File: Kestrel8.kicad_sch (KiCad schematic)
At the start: 0 parts

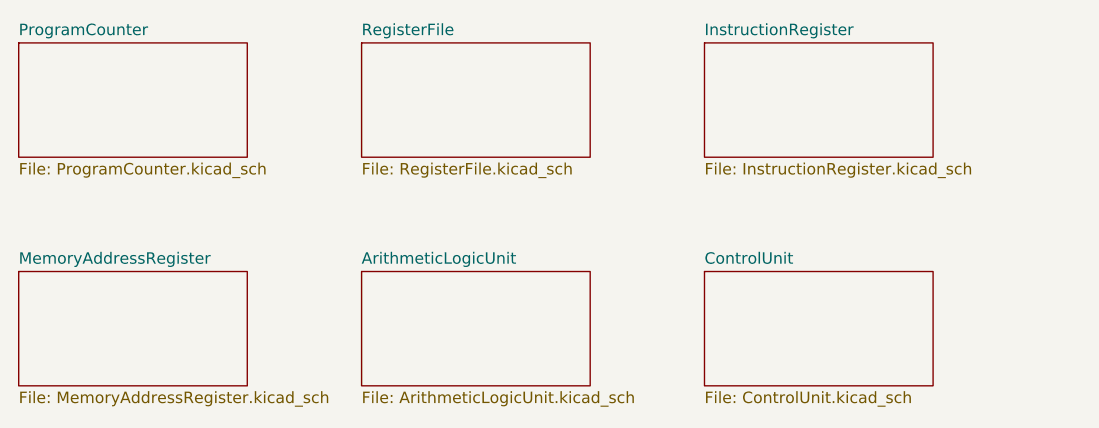
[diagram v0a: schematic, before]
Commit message: Cleans up and restructures schematics
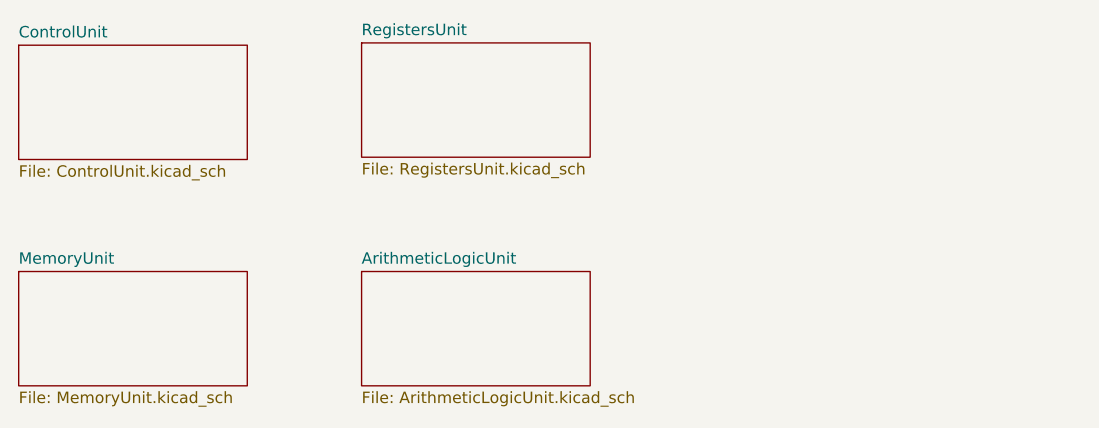
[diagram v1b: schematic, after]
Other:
- sheet MemoryAddressRegister renamed MemoryUnit
- sheet RegisterFile renamed RegistersUnit
- removed sheet InstructionRegister
- removed sheet ProgramCounter
- sheet MemoryUnit: file MemoryAddressRegister.kicad_sch -> MemoryUnit.kicad_sch
- sheet RegistersUnit: file RegisterFile.kicad_sch -> RegistersUnit.kicad_sch
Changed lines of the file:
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@@
 			(color 0 0 0 0.0000)
 		)
-		(property "Sheetname" "MemoryAddressRegister"
+		(property "Sheetname" "MemoryUnit"
 			(at 25.4 50.0884 0)
 			(effects
@@
 			)
 		)
-		(property "Sheetfile" "MemoryAddressRegister.kicad_sch"
+		(property "Sheetfile" "MemoryUnit.kicad_sch"
 			(at 25.4 64.0846 0)
 			(effects
@@
 			(color 0 0 0 0.0000)
 		)
-		(property "Sheetname" "RegisterFile"
+		(property "Sheetname" "RegistersUnit"
 			(at 63.5 24.6884 0)
 			(effects
@@
 			)
 		)
-		(property "Sheetfile" "RegisterFile.kicad_sch"
+		(property "Sheetfile" "RegistersUnit.kicad_sch"
 			(at 63.5 38.6846 0)
 			(effects
@@
 				(path "/afdf0bd2-bb31-4132-9ca5-f1f94e74d630"
 					(page "3")
-				)
-			)
-		)
-	)
-	(sheet
-		(at 101.6 25.4)
-		(size 25.4 12.7)
-		(exclude_from_sim no)
-		(in_bom yes)
-		(on_board yes)
-		(dnp no)
-		(fields_autoplaced yes)
-		(stroke
-			(width 0.1524)
-			(type solid)
-		)
-		(fill
-			(color 0 0 0 0.0000)
-		)
-		(property "Sheetname" "InstructionRegister"
-			(at 101.6 24.6884 0)
-			(effects
-				(font
-					(size 1.27 1.27)
-				)
-				(justify left bottom)
-			)
-		)
-		(property "Sheetfile" "InstructionRegister.kicad_sch"
-			(at 101.6 38.6846 0)
-			(effects
-				(font
-					(size 1.27 1.27)
-				)
-				(justify left top)
-			)
-		)
-		(instances
-			(project "Kestrel8"
-				(path "/afdf0bd2-bb31-4132-9ca5-f1f94e74d630"
-					(page "4")
-				)
-			)
-		)
-	)
-	(sheet
-		(at 25.4 25.4)
-		(size 25.4 12.7)
-		(exclude_from_sim no)
-		(in_bom yes)
-		(on_board yes)
-		(dnp no)
-		(fields_autoplaced yes)
-		(stroke
-			(width 0.1524)
-			(type solid)
-		)
-		(fill
-			(color 0 0 0 0.0000)
-		)
-		(property "Sheetname" "ProgramCounter"
-			(at 25.4 24.6884 0)
-			(effects
-				(font
-					(size 1.27 1.27)
-				)
-				(justify left bottom)
-			)
-		)
-		(property "Sheetfile" "ProgramCounter.kicad_sch"
-			(at 25.4 38.6846 0)
-			(effects
-				(font
-					(size 1.27 1.27)
-				)
-				(justify left top)
-			)
-		)
-		(instances
-			(project "Kestrel8"
-				(path "/afdf0bd2-bb31-4132-9ca5-f1f94e74d630"
-					(page "2")
 				)
 			)
@@
 	)
 	(sheet
-		(at 101.6 50.8)
+		(at 25.4 25.654)
 		(size 25.4 12.7)
 		(exclude_from_sim no)
@@
 		)
 		(property "Sheetname" "ControlUnit"
-			(at 101.6 50.0884 0)
+			(at 25.4 24.9424 0)
 			(effects
 				(font
@@
 		)
 		(property "Sheetfile" "ControlUnit.kicad_sch"
-			(at 101.6 64.0846 0)
+			(at 25.4 38.9386 0)
 			(effects
 				(font
